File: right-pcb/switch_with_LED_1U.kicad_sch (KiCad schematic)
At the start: 4 parts

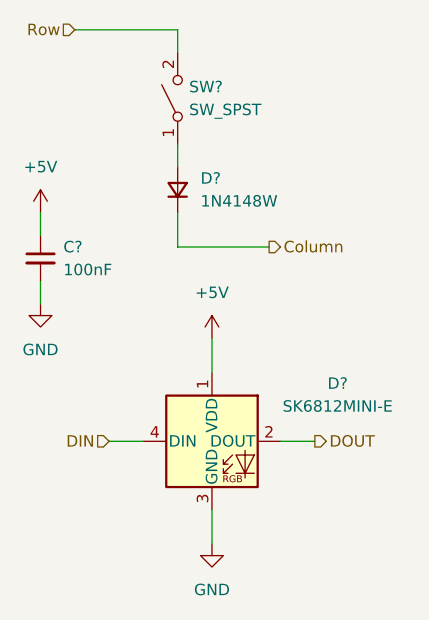
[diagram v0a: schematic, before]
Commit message: initial placement of switches and modifications from left to right
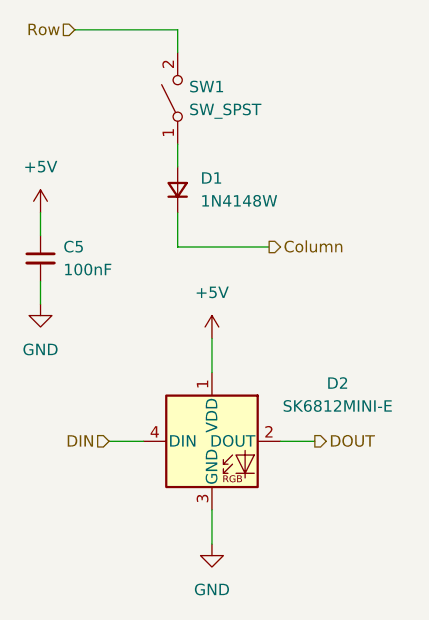
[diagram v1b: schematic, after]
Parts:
- gave numbers to parts that had none: 4

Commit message: Boards were ordered
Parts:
- SW1: symbol Switch:SW_SPST -> SW-gElectroMech:SPST_MOM
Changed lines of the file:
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@@
 	)
 	(symbol
-		(lib_id "Switch:SW_SPST")
+		(lib_id "SW-gElectroMech:SPST_MOM")
 		(at 120.65 93.98 90)
 		(unit 1)
@@
 		)
 		(property "Datasheet" ""
-			(at 120.65 93.98 0)
+			(at 115.57 93.98 0)
 			(hide yes)
 			(show_name no)
@@
 			)
 		)
-		(property "Description" "Single Pole Single Throw (SPST) switch"
+		(property "Description" "Push button switch, generic, two pins"
 			(at 120.65 93.98 0)
 			(hide yes)
